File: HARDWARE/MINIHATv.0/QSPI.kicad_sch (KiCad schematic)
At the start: 9 parts, among them U3 W25Q128JVS

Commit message: editorial changes
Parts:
- renumbered C11 to C51, R32 to R69, R33 to R70, R34 to R71, R35 to R72, R36 to R73, R37 to R74, R38 to R75, U3 to U8
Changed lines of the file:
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@@
 				(size 1.27 1.27)
 			)
-			(justify right)
+			(justify left)
 		)
 	)
@@
 		(in_pos_files yes)
 		(dnp no)
-		(property "Reference" "R34"
+		(property "Reference" "R71"
 			(at 79.502 76.2 90)
 			(show_name no)
@@
 		(dnp no)
 		(fields_autoplaced yes)
-		(property "Reference" "#PWR028"
+		(property "Reference" "#PWR0114"
 			(at 105.41 64.77 0)
 			(hide yes)
@@
 		(dnp no)
 		(fields_autoplaced yes)
-		(property "Reference" "#PWR029"
+		(property "Reference" "#PWR0113"
 			(at 124.46 78.74 0)
 			(hide yes)
@@
 		(in_pos_files yes)
 		(dnp no)
-		(property "Reference" "R37"
+		(property "Reference" "R74"
 			(at 79.502 83.82 90)
 			(show_name no)
@@
 		(dnp no)
 		(fields_autoplaced yes)
-		(property "Reference" "C11"
+		(property "Reference" "C51"
 			(at 128.27 66.0399 0)
 			(show_name no)
@@
 		(dnp no)
 		(fields_autoplaced yes)
-		(property "Reference" "#PWR027"
+		(property "Reference" "#PWR0115"
 			(at 105.41 102.87 0)
 			(hide yes)
@@
 		(in_pos_files yes)
 		(dnp no)
-		(property "Reference" "R35"
+		(property "Reference" "R72"
 			(at 79.502 78.74 90)
 			(show_name no)
@@
 		(in_pos_files yes)
 		(dnp no)
-		(property "Reference" "R32"
+		(property "Reference" "R69"
 			(at 79.502 71.12 90)
 			(show_name no)
@@
 		(in_pos_files yes)
 		(dnp no)
-		(property "Reference" "R38"
+		(property "Reference" "R75"
 			(at 96.012 68.58 0)
 			(show_name no)
@@
 		(in_pos_files yes)
 		(dnp no)
-		(property "Reference" "R36"
+		(property "Reference" "R73"
 			(at 79.502 81.28 90)
 			(show_name no)
@@
 		(dnp no)
 		(fields_autoplaced yes)
-		(property "Reference" "U3"
+		(property "Reference" "U8"
 			(at 116.84 78.7399 0)
 			(show_name no)
@@
 		(in_pos_files yes)
 		(dnp no)
-		(property "Reference" "R33"
+		(property "Reference" "R70"
 			(at 79.502 73.66 90)
 			(show_name no)

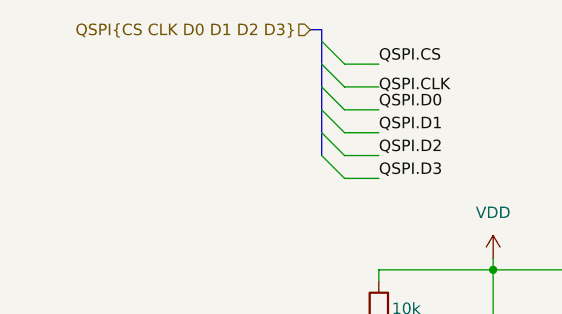
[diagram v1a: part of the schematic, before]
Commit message: added sdram and usb pages to top page
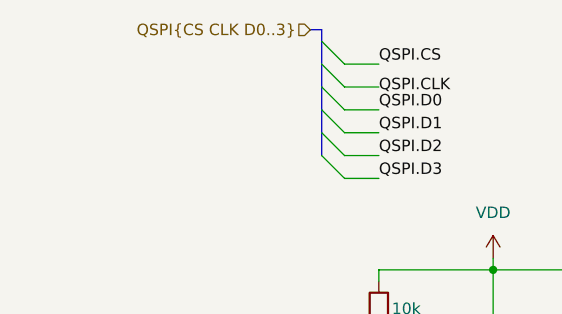
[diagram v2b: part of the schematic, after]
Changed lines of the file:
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@@
 		)
 	)
-	(hierarchical_label "QSPI{CS CLK D0 D1 D2 D3}"
+	(hierarchical_label "QSPI{CS CLK D0..3}"
 		(shape input)
 		(at 85.09 35.56 180)

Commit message: mcu pwr/vcap ports, hdmi gpio, buses
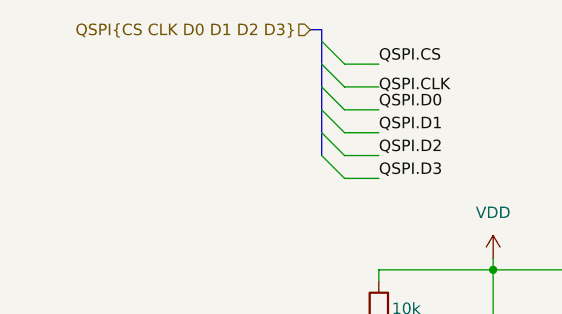
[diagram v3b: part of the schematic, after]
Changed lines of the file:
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@@
 		)
 	)
-	(hierarchical_label "QSPI{CS CLK D0..3}"
+	(hierarchical_label "QSPI{CS CLK D0 D1 D2 D3}"
 		(shape input)
 		(at 85.09 35.56 180)
